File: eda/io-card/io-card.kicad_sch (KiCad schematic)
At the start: 22 parts, among them J3 PortA, J4 PortB, J5 ControlLines, J6 SPI, U1 W65C22SxP, U13 74HCT138, U2 W65C22SxP, U3 74HCT14, U5 74HCT00

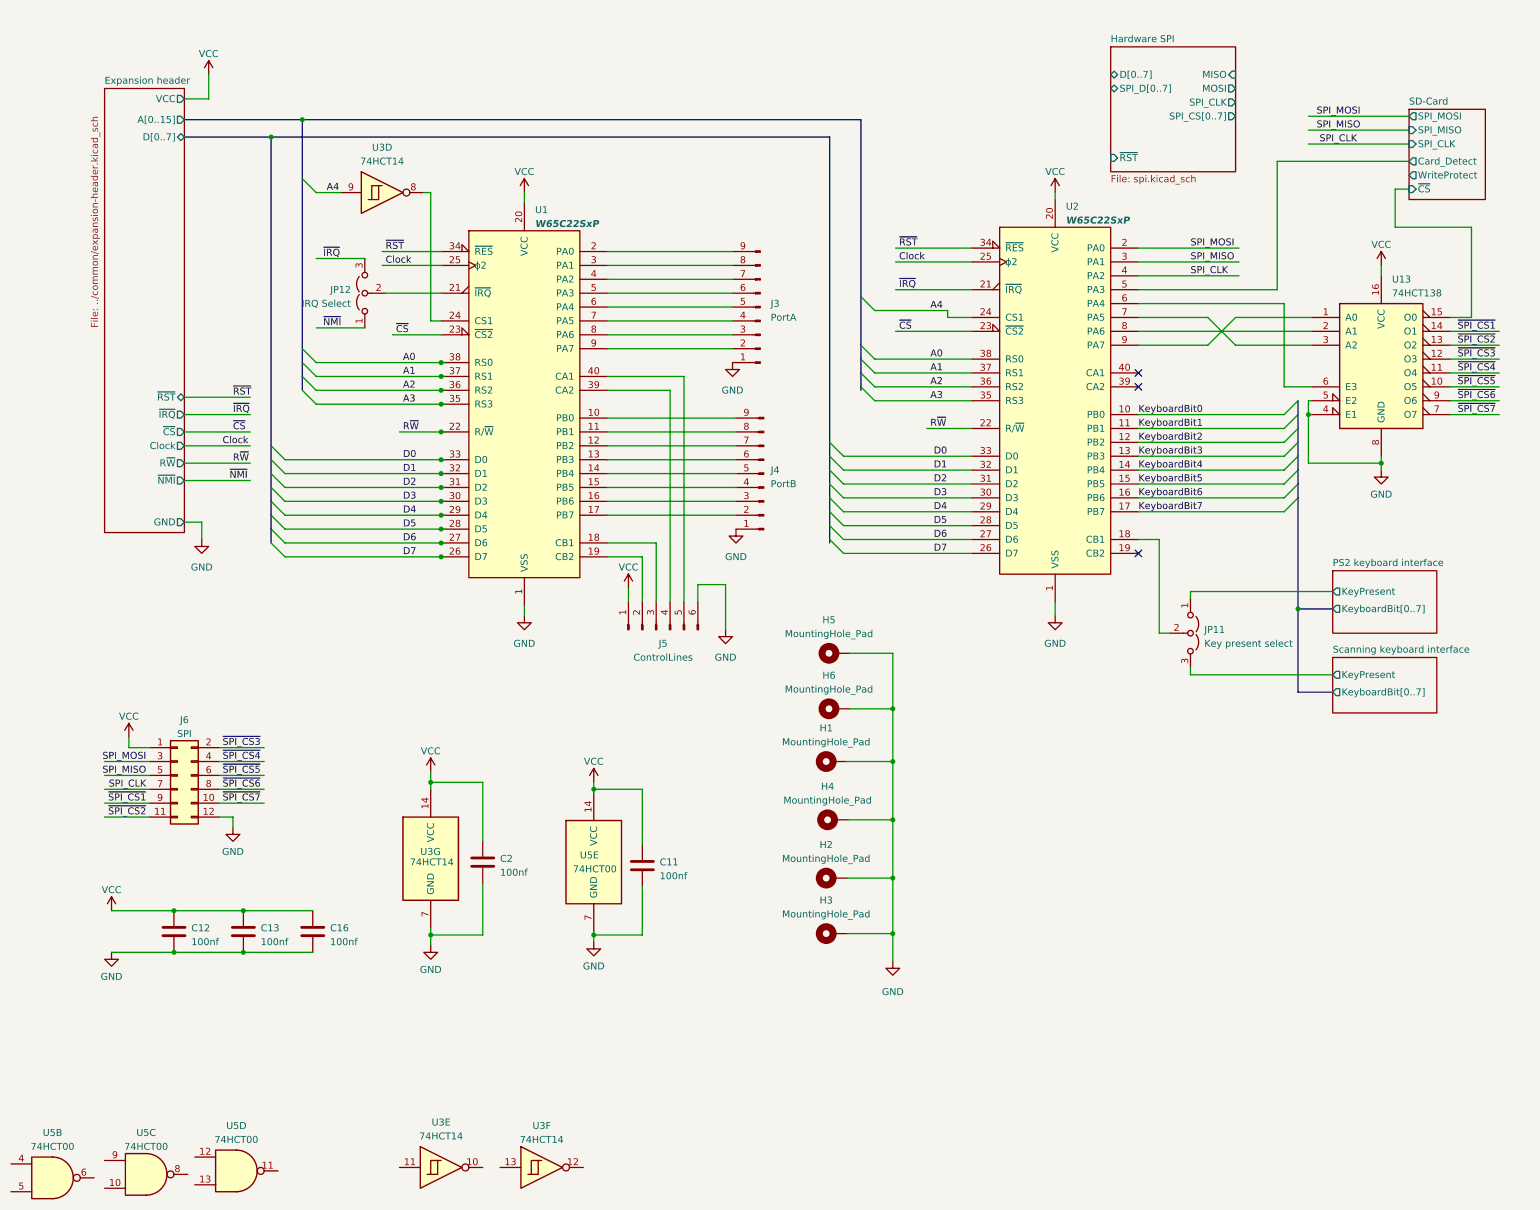
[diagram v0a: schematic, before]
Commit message: Add address decode
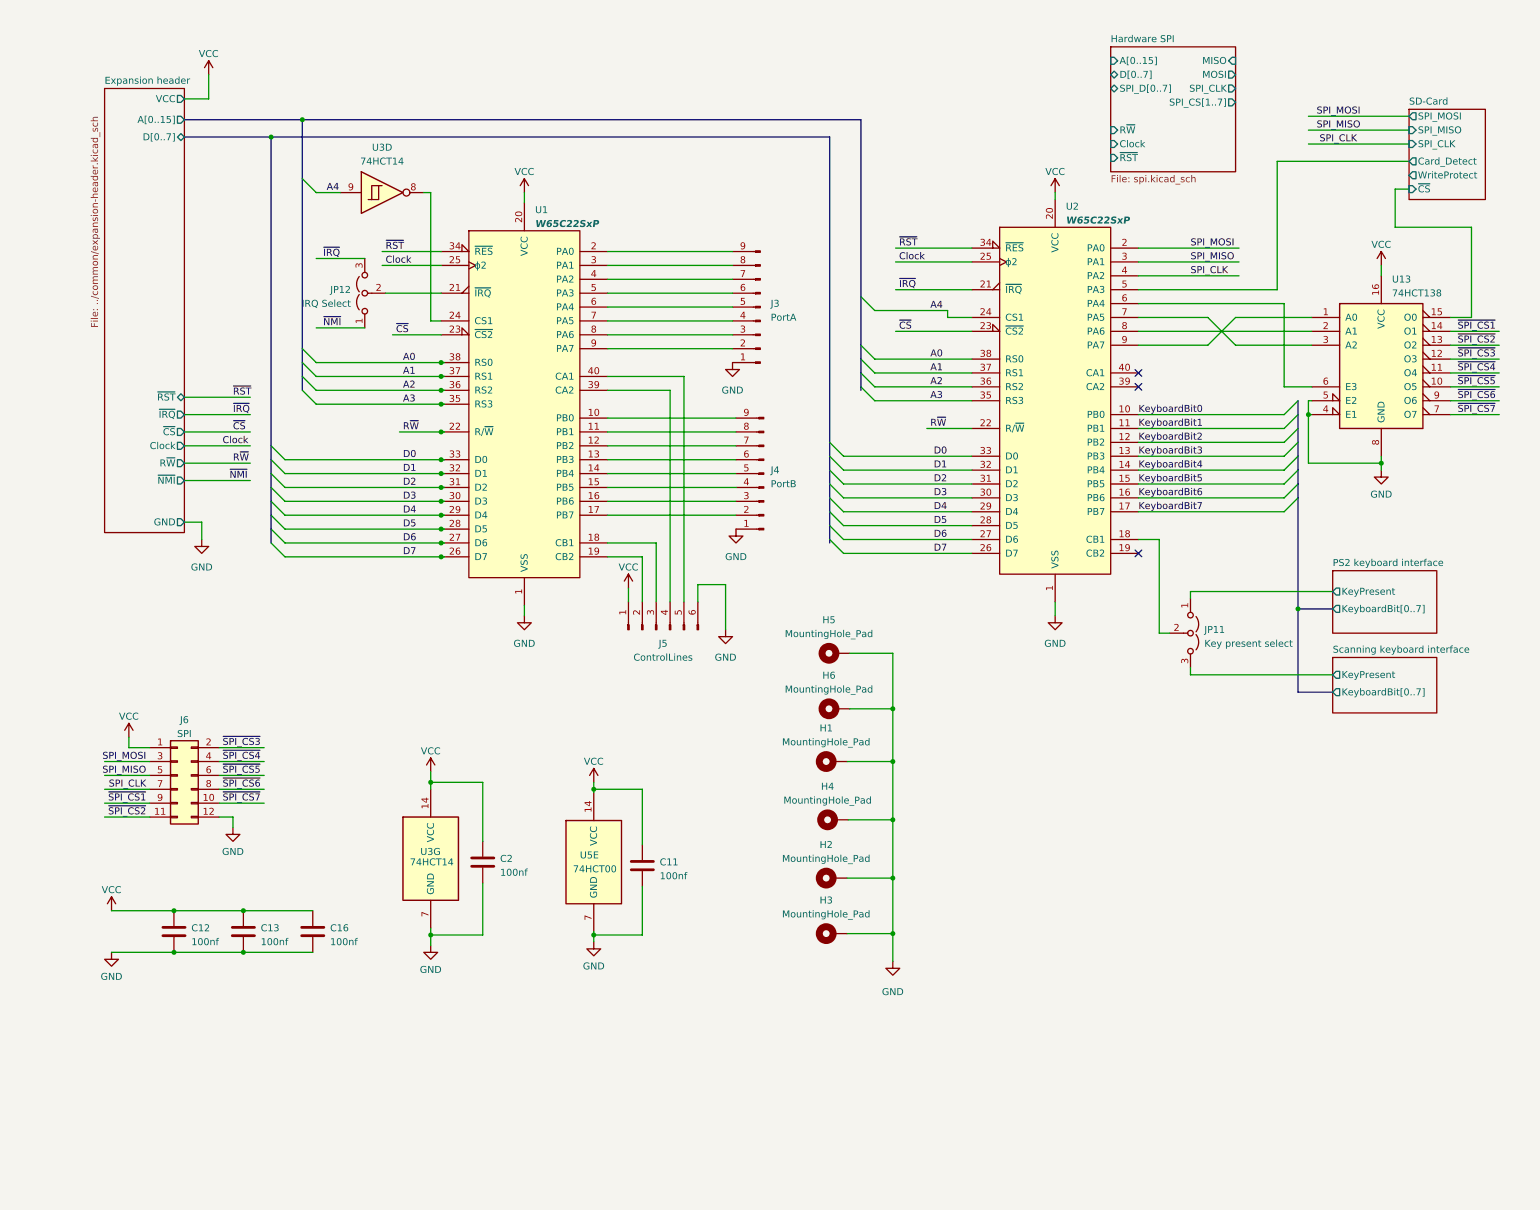
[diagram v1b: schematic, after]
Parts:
- removed unit 5 of U3
- removed unit 6 of U3
- removed unit 3 of U5
- removed unit 4 of U5
- removed unit 2 of U5
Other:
- sheet Hardware SPI ports: added A[0..15], Clock, R~{W}, SPI_CS[1..7]; removed SPI_CS[0..7]

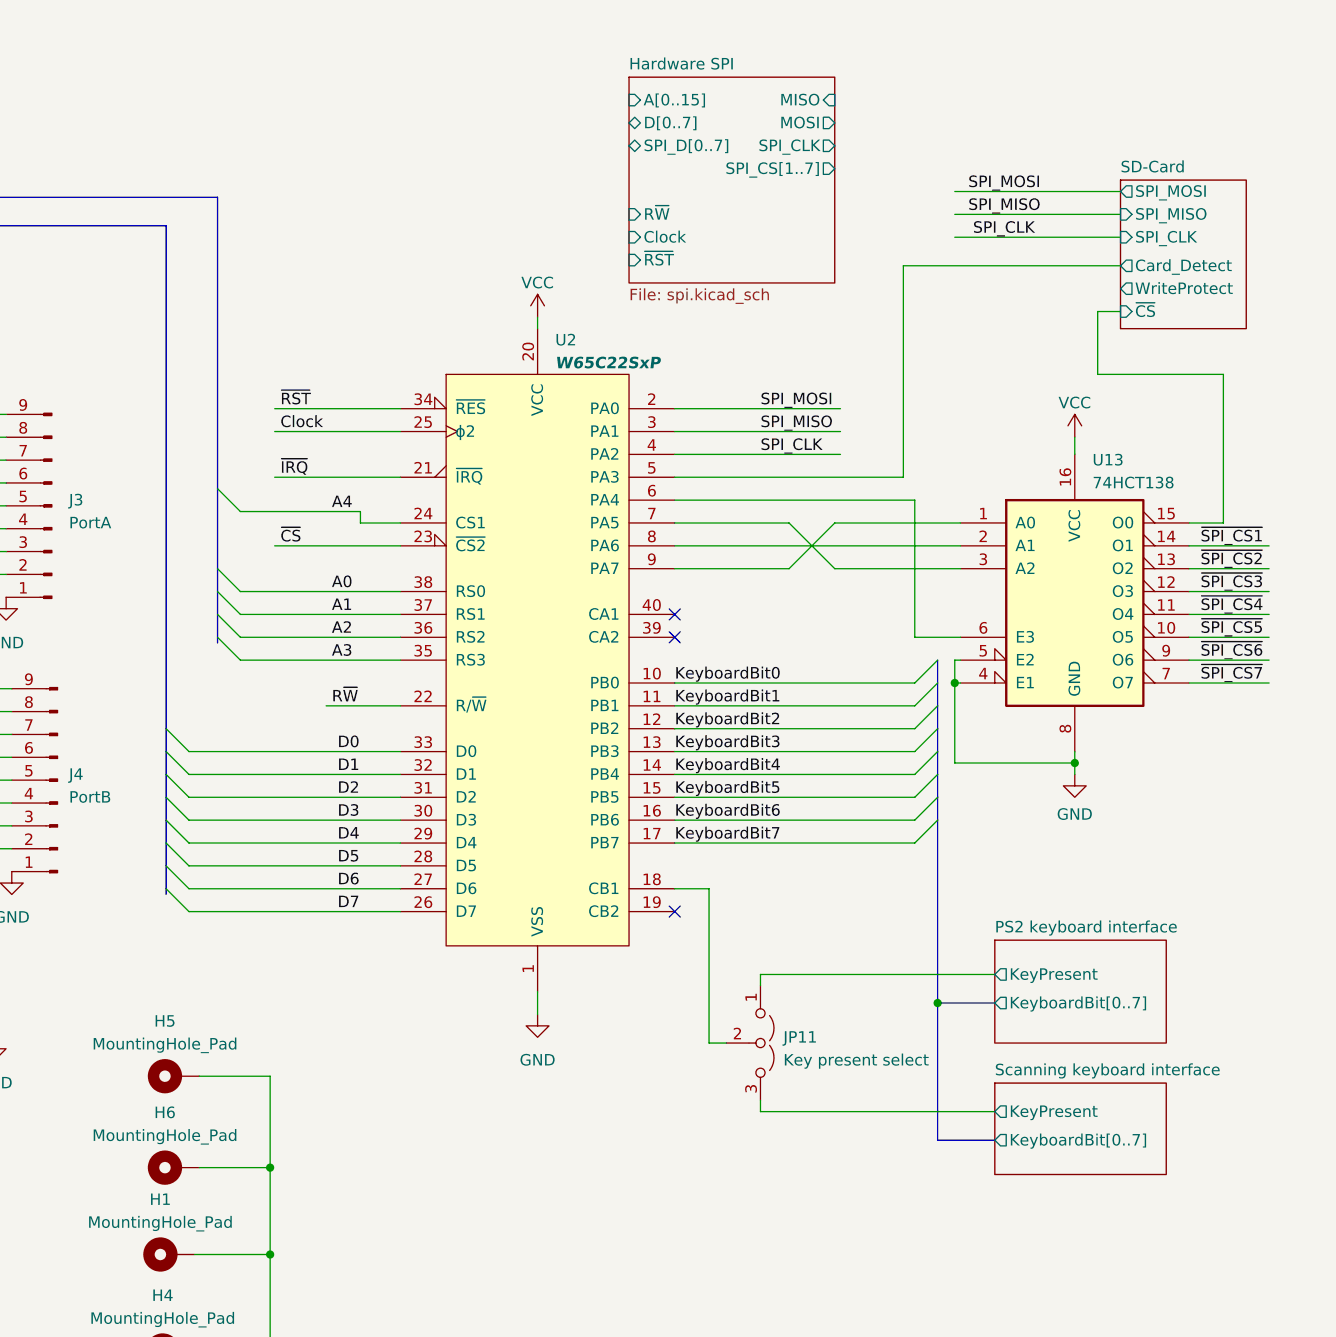
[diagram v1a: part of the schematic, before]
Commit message: Add memcontrol display to panels
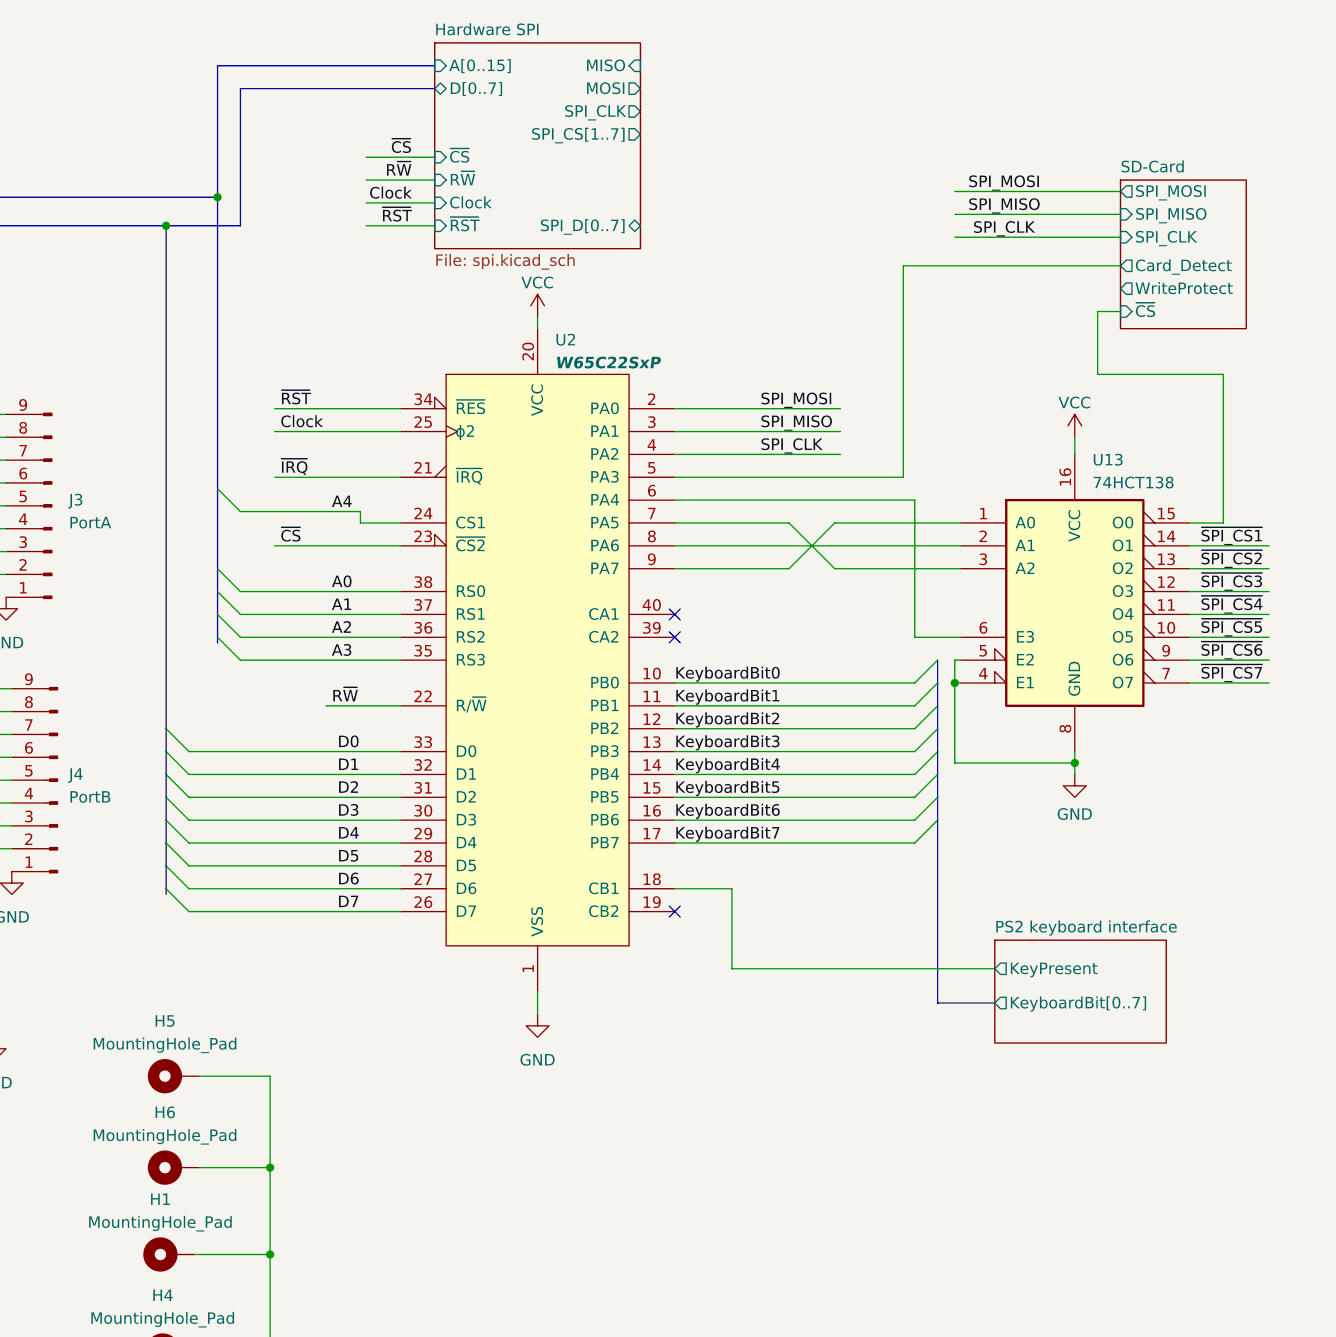
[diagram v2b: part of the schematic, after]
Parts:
- removed JP11: Key present select, Connector_PinHeader_2.54mm:PinHeader_1x03_P2.54mm_Vertical, symbol Jumper:Jumper_3_Open
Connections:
- net PS2 keyboard interface/KeyPresent: now also U2.18 (CB1)
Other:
- removed sheet Scanning keyboard interface
- sheet Hardware SPI ports: added ~{CS}; removed none
